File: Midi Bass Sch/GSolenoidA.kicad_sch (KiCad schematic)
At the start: 105 parts, among them Q73 BDW93C, Q74 BDW93C, Q75 BDW93C, Q76 BDW93C, Q77 BDW93C, Q78 BDW93C, Q79 BDW93C, Q80 BDW93C, Q81 BDW93C, Q82 BDW93C, Q83 BDW93C, Q84 BDW93C, Q85 BDW93C, Q86 BDW93C, Q87 BDW93C, Q88 BDW93C, Q89 BDW93C, Q90 BDW93C, Q91 BDW93C, Q92 BDW93C, U26 LTV-247, U27 LTV-247, U28 LTV-247, U29 LTV-247, U30 LTV-247

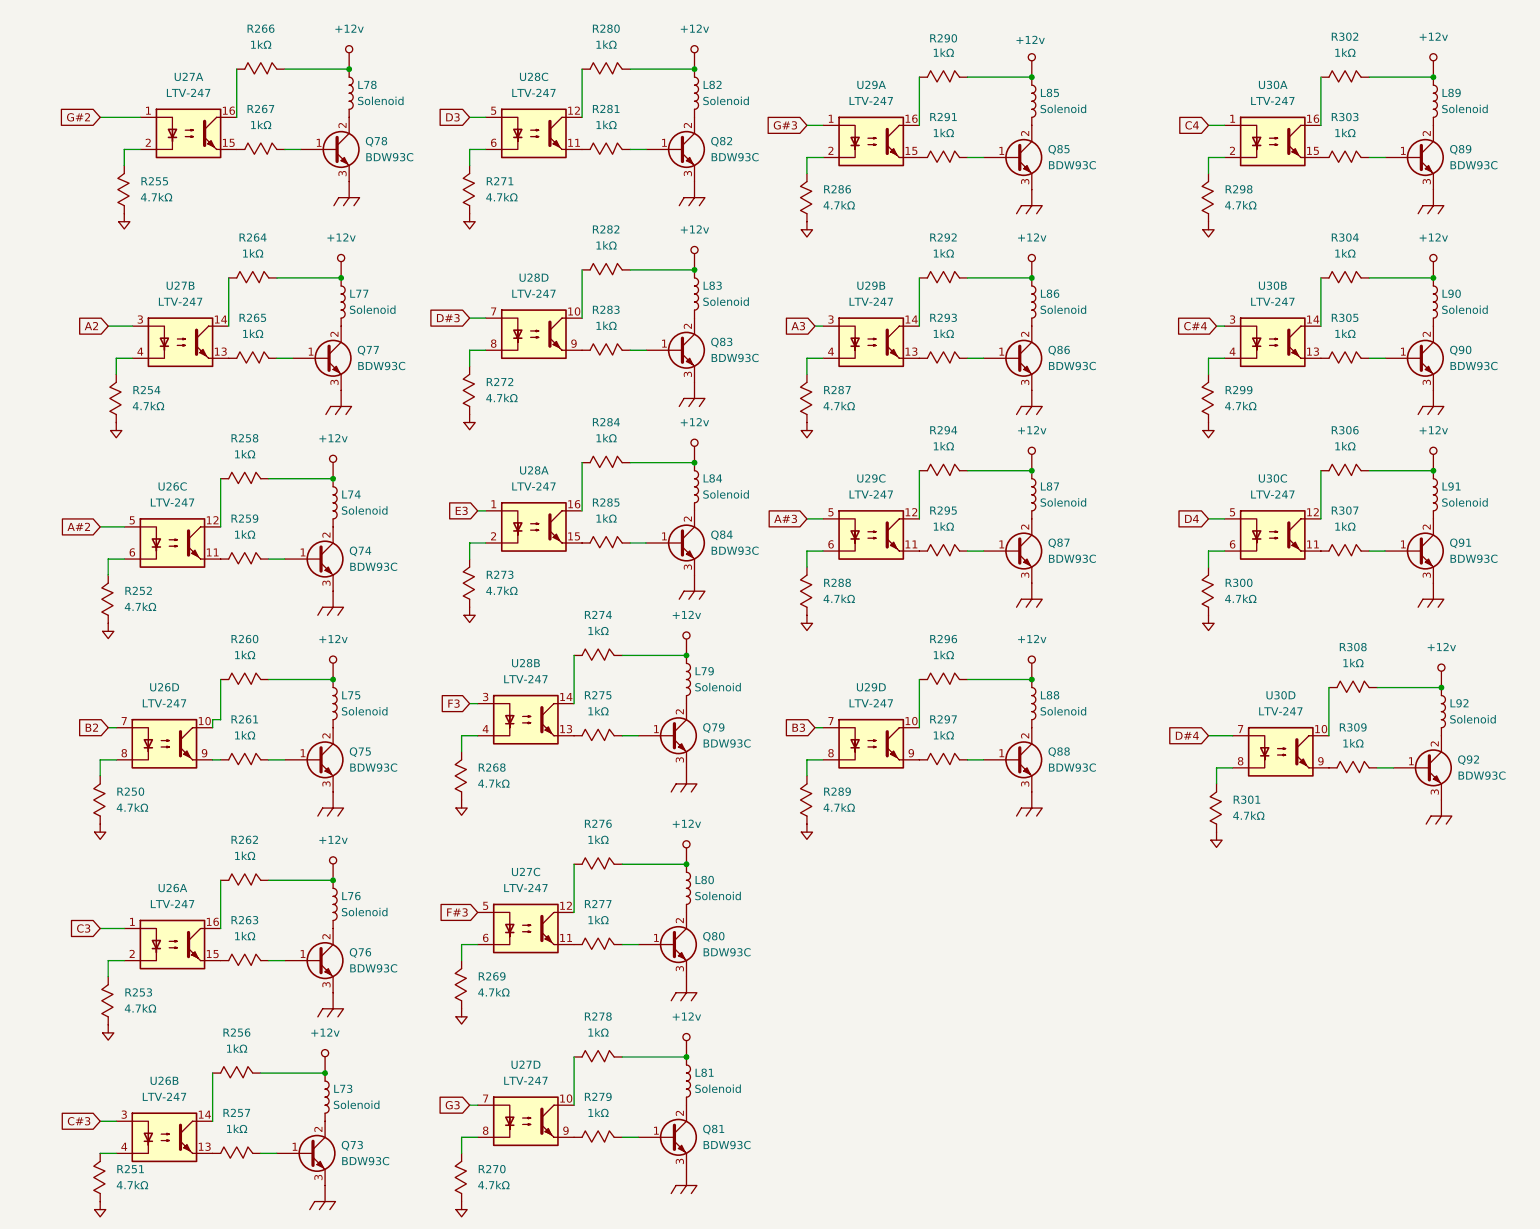
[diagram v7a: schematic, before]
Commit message: changed transistor for schematic
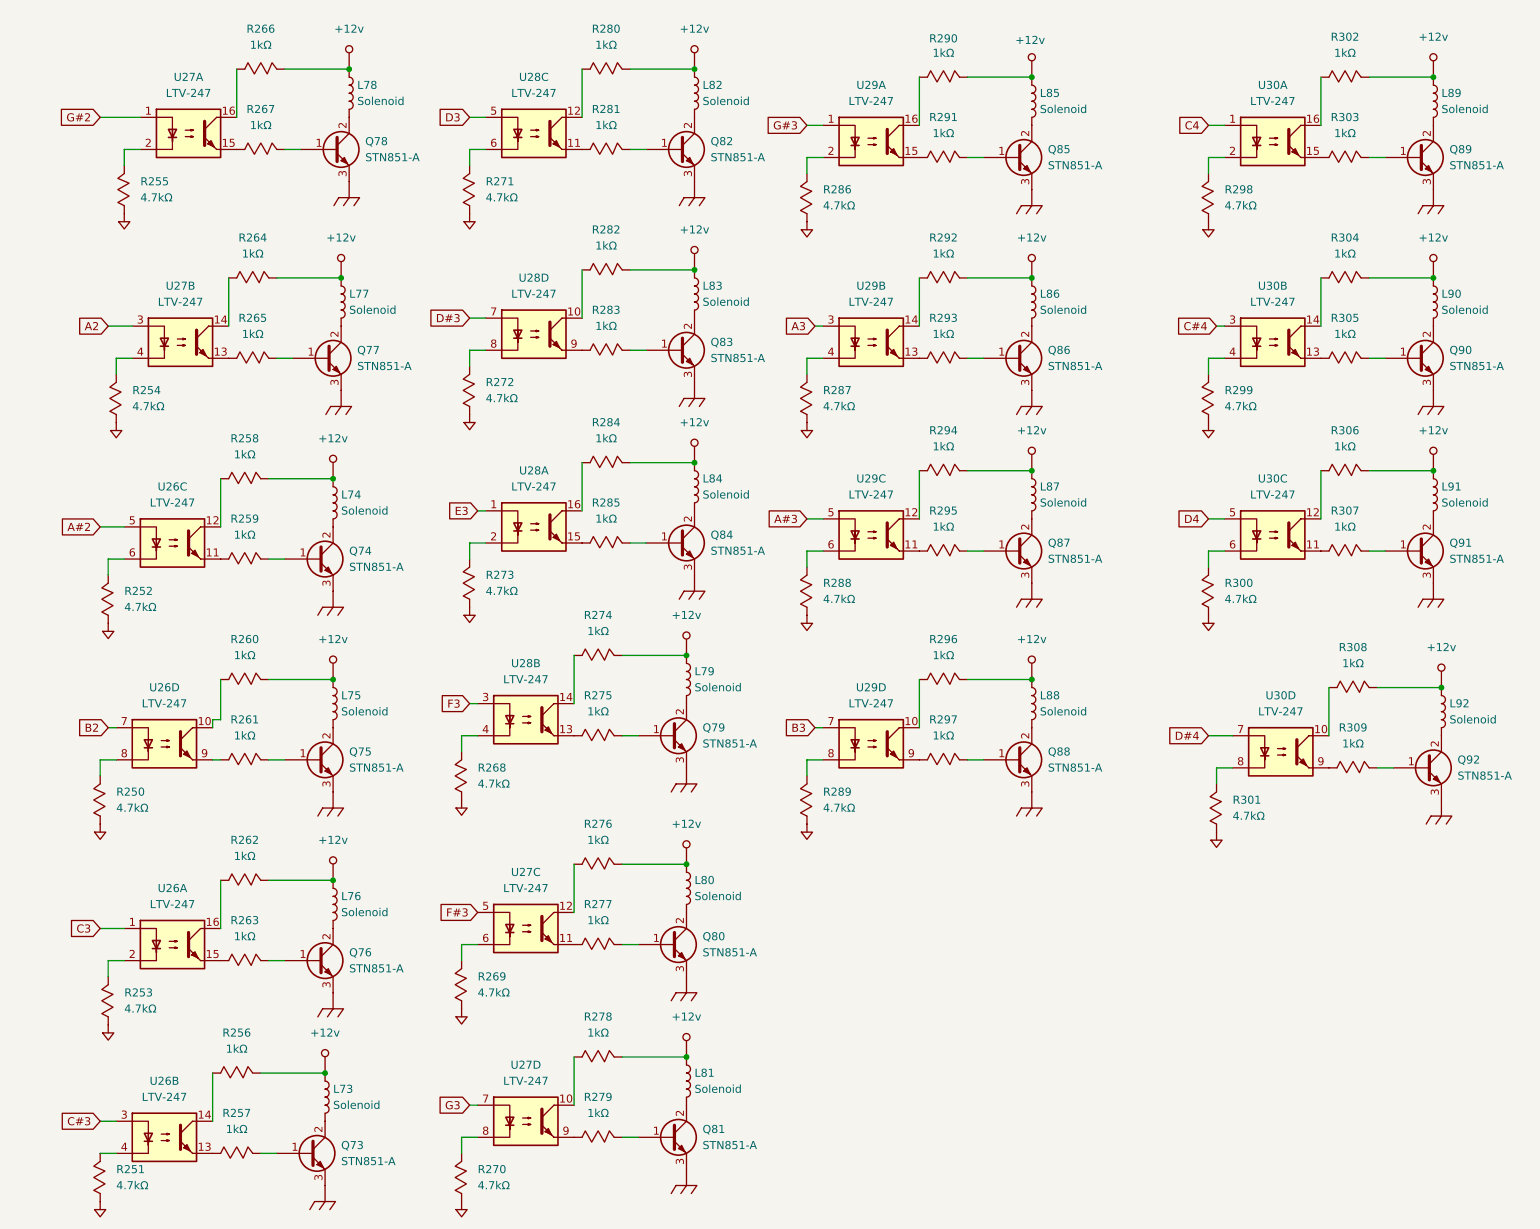
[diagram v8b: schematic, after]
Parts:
- Q73, Q74, Q75, Q76, Q77, Q78, Q79, Q80, Q81, Q82, Q83, Q84, Q85, Q86, Q87, Q88, Q89, Q90, Q91, Q92: value BDW93C -> STN851-A
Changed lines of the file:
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@@
 			)
 		)
-		(property "Value" "BDW93C"
+		(property "Value" "STN851-A"
 			(at 243.84 36.8299 0)
 			(effects
@@
 			)
 		)
-		(property "Value" "BDW93C"
+		(property "Value" "STN851-A"
 			(at 68.58 194.3099 0)
 			(effects
@@
 			)
 		)
-		(property "Value" "BDW93C"
+		(property "Value" "STN851-A"
 			(at 69.85 100.3299 0)
 			(effects
@@
 			)
 		)
-		(property "Value" "BDW93C"
+		(property "Value" "STN851-A"
 			(at 180.34 36.8299 0)
 			(effects
@@
 			)
 		)
-		(property "Value" "BDW93C"
+		(property "Value" "STN851-A"
 			(at 180.34 68.5799 0)
 			(effects
@@
 			)
 		)
-		(property "Value" "BDW93C"
+		(property "Value" "STN851-A"
 			(at 180.34 132.0799 0)
 			(effects
@@
 			)
 		)
-		(property "Value" "BDW93C"
+		(property "Value" "STN851-A"
 			(at 125.73 191.7699 0)
 			(effects
@@
 			)
 		)
-		(property "Value" "BDW93C"
+		(property "Value" "STN851-A"
 			(at 243.84 99.0599 0)
 			(effects
@@
 			)
 		)
-		(property "Value" "BDW93C"
+		(property "Value" "STN851-A"
 			(at 69.85 163.8299 0)
 			(effects
@@
 			)
 		)
-		(property "Value" "BDW93C"
+		(property "Value" "STN851-A"
 			(at 125.73 128.2699 0)
 			(effects
@@
 			)
 		)
-		(property "Value" "BDW93C"
+		(property "Value" "STN851-A"
 			(at 127 35.5599 0)
 			(effects
@@
 			)
 		)
-		(property "Value" "BDW93C"
+		(property "Value" "STN851-A"
 			(at 69.85 132.0799 0)
 			(effects
@@
 			)
 		)
-		(property "Value" "BDW93C"
+		(property "Value" "STN851-A"
 			(at 127 67.3099 0)
 			(effects
@@
 			)
 		)
-		(property "Value" "BDW93C"
+		(property "Value" "STN851-A"
 			(at 72.39 35.5599 0)
 			(effects
@@
 			)
 		)
-		(property "Value" "BDW93C"
+		(property "Value" "STN851-A"
 			(at 71.12 68.5799 0)
 			(effects
@@
 			)
 		)
-		(property "Value" "BDW93C"
+		(property "Value" "STN851-A"
 			(at 180.34 99.0599 0)
 			(effects
@@
 			)
 		)
-		(property "Value" "BDW93C"
+		(property "Value" "STN851-A"
 			(at 127 97.7899 0)
 			(effects
@@
 			)
 		)
-		(property "Value" "BDW93C"
+		(property "Value" "STN851-A"
 			(at 125.73 161.2899 0)
 			(effects
@@
 			)
 		)
-		(property "Value" "BDW93C"
+		(property "Value" "STN851-A"
 			(at 245.11 133.3499 0)
 			(effects
@@
 			)
 		)
-		(property "Value" "BDW93C"
+		(property "Value" "STN851-A"
 			(at 243.84 68.5799 0)
 			(effects
